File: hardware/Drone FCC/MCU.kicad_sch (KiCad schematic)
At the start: 38 parts, among them SW101 SW RESET, U101 STM32F746ZGTx, Y101 12MHz, Y102 32.768kHz

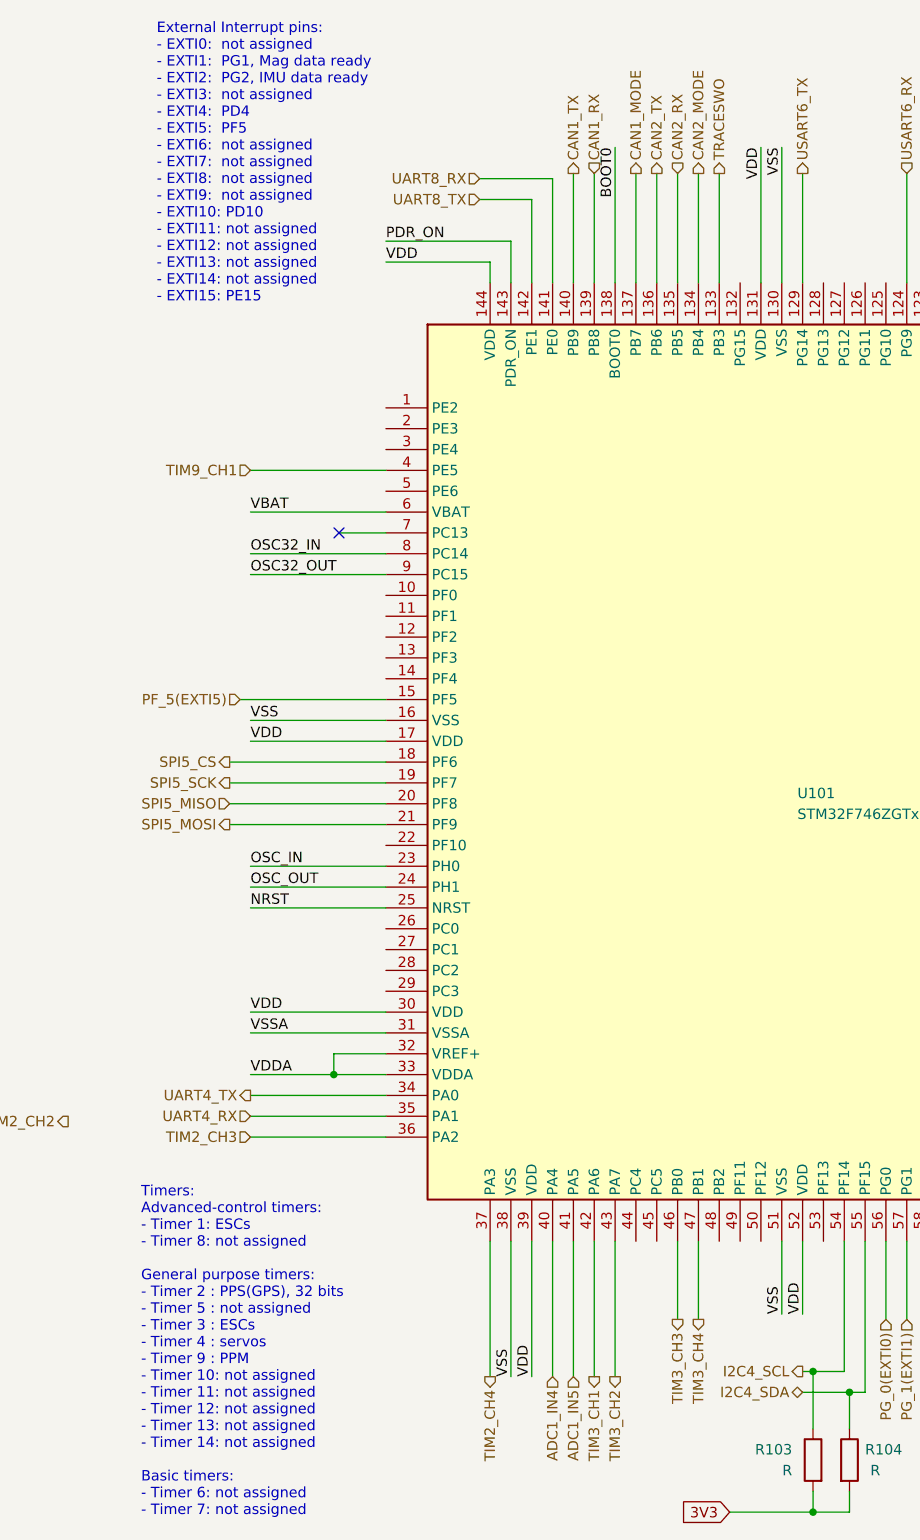
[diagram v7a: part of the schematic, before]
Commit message: added LEDs in routing
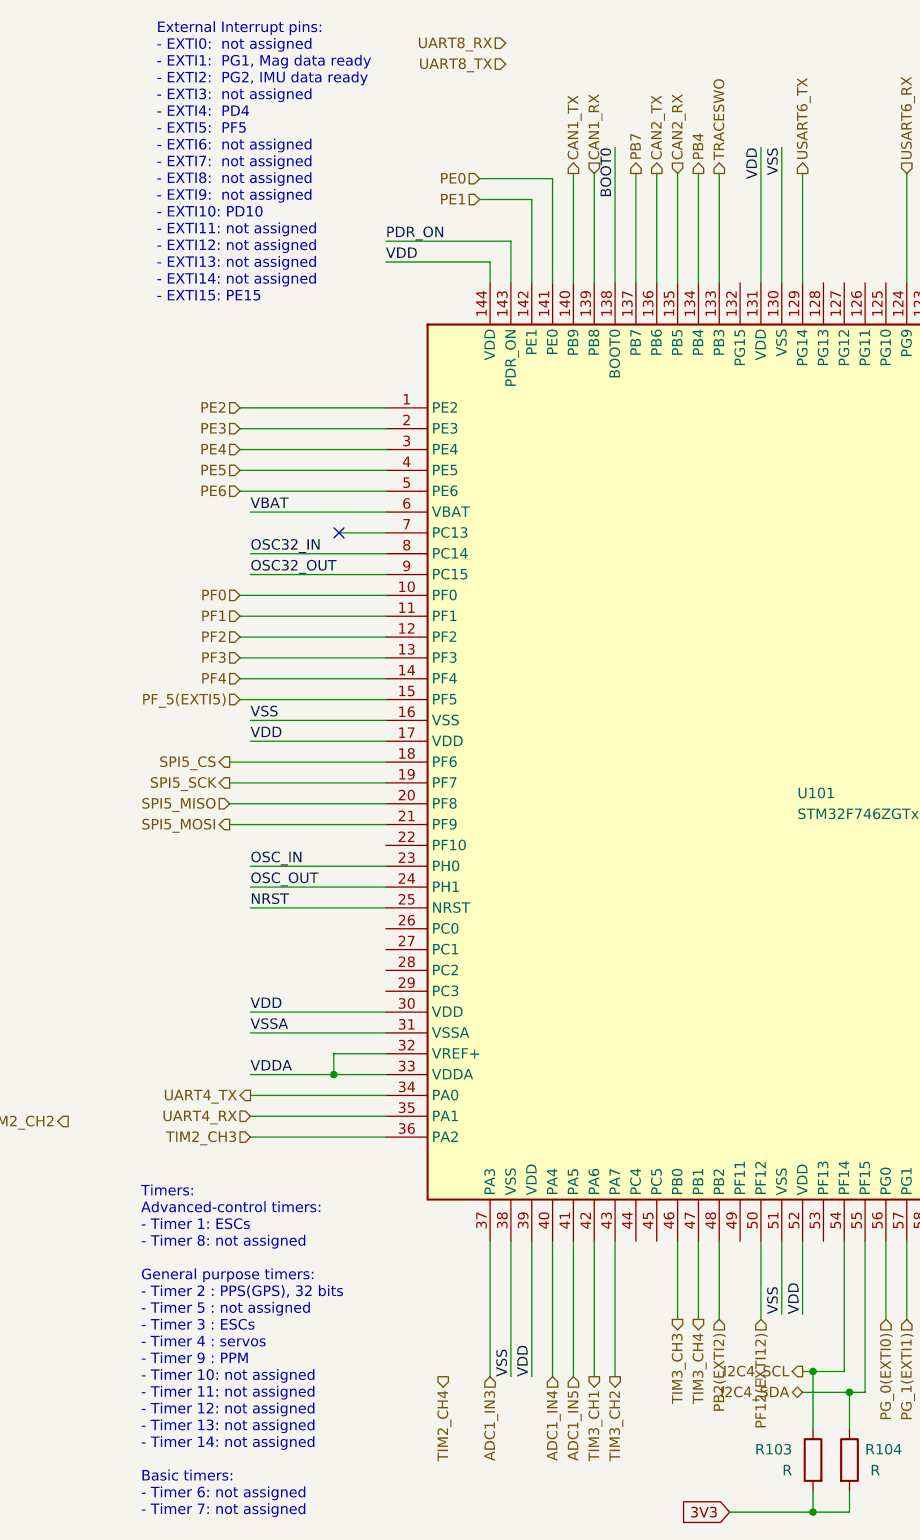
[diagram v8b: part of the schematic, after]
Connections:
- net TIM2_CH4: no longer U101.37 (PA3)
- net UART8_RX: no longer U101.141 (PE0)
- net UART8_TX: no longer U101.142 (PE1)
- net PE2: now reaches U101.1 (PE2)
- net PF0: now reaches U101.10 (PF0)
- net PF1: now reaches U101.11 (PF1)
- net PF2: now reaches U101.12 (PF2)
- net PF3: now reaches U101.13 (PF3)
- net PF4: now reaches U101.14 (PF4)
- net PE3: now reaches U101.2 (PE3)
- net PE4: now reaches U101.3 (PE4)
- net PB2(EXTI2): now reaches U101.48 (PB2)
- net PE6: now reaches U101.5 (PE6)
- net PF12(EXTI12): now reaches U101.50 (PF12)
- net CAN1_MODE renamed PB7
- net CAN2_MODE renamed PB4
- net TIM9_CH1 renamed PE5
- new net ADC1_IN3: U101.37 (PA3)
- new net PE0: U101.141 (PE0)
- new net PE1: U101.142 (PE1)
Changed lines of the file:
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@@
+    (stroke (width 0) (type default) (color 0 0 0 0))
+  )
+  (wire (pts (xy 25.4 66.04) (xy 43.18 66.04))
     (stroke (width 0) (type default) (color 0 0 0 0))
   )
@@
     (stroke (width 0) (type default) (color 0 0 0 0))
   )
+  (wire (pts (xy 25.4 93.98) (xy 43.18 93.98))
+    (stroke (width 0) (type default) (color 0 0 0 0))
+  )
   (wire (pts (xy 139.7 195.58) (xy 149.225 195.58))
     (stroke (width 0) (type default) (color 0 0 0 0))
@@
     (stroke (width 0) (type default) (color 0 0 0 0))
   )
+  (wire (pts (xy 83.82 162.56) (xy 83.82 172.085))
+    (stroke (width 0) (type default) (color 0 0 0 0))
+  )
   (wire (pts (xy 93.98 162.56) (xy 93.98 171.45))
     (stroke (width 0) (type default) (color 0 0 0 0))
@@
     (stroke (width 0) (type default) (color 0 0 0 0))
   )
+  (wire (pts (xy 25.4 60.96) (xy 43.18 60.96))
+    (stroke (width 0) (type default) (color 0 0 0 0))
+  )
   (wire (pts (xy 58.42 179.07) (xy 58.42 162.56))
     (stroke (width 0) (type default) (color 0 0 0 0))
@@
     (stroke (width 0) (type default) (color 0 0 0 0))
   )
+  (wire (pts (xy 88.9 162.56) (xy 88.9 172.085))
+    (stroke (width 0) (type default) (color 0 0 0 0))
+  )
   (wire (pts (xy 274.32 81.915) (xy 274.32 83.82))
     (stroke (width 0) (type default) (color 0 0 0 0))
@@
     (stroke (width 0) (type default) (color 0 0 0 0))
   )
+  (wire (pts (xy 25.4 86.36) (xy 43.18 86.36))
+    (stroke (width 0) (type default) (color 0 0 0 0))
+  )
   (wire (pts (xy 259.08 49.53) (xy 270.51 49.53))
     (stroke (width 0) (type default) (color 0 0 0 0))
@@
     (stroke (width 0) (type default) (color 0 0 0 0))
   )
+  (wire (pts (xy 25.4 71.12) (xy 43.18 71.12))
+    (stroke (width 0) (type default) (color 0 0 0 0))
+  )
   (wire (pts (xy 270.51 38.1) (xy 270.51 36.195))
     (stroke (width 0) (type default) (color 0 0 0 0))
@@
     (stroke (width 0) (type default) (color 0 0 0 0))
   )
-  (wire (pts (xy 26.67 68.58) (xy 43.18 68.58))
-    (stroke (width 0) (type default) (color 0 0 0 0))
-  )
   (wire (pts (xy 139.7 180.975) (xy 153.67 180.975))
     (stroke (width 0) (type default) (color 0 0 0 0))
@@
     (stroke (width 0) (type default) (color 0 0 0 0))
   )
+  (wire (pts (xy 25.4 91.44) (xy 43.18 91.44))
+    (stroke (width 0) (type default) (color 0 0 0 0))
+  )
   (wire (pts (xy 236.22 36.195) (xy 236.22 38.1))
     (stroke (width 0) (type default) (color 0 0 0 0))
@@
     (stroke (width 0) (type default) (color 0 0 0 0))
   )
+  (wire (pts (xy 25.4 88.9) (xy 43.18 88.9))
+    (stroke (width 0) (type default) (color 0 0 0 0))
+  )
   (polyline (pts (xy 202.565 112.395) (xy 204.47 112.395))
     (stroke (width 0) (type default) (color 0 0 0 0))
@@
     (stroke (width 0) (type default) (color 0 0 0 0))
   )
+  (wire (pts (xy 25.4 68.58) (xy 43.18 68.58))
+    (stroke (width 0) (type default) (color 0 0 0 0))
+  )
   (wire (pts (xy 165.735 29.845) (xy 173.99 29.845))
     (stroke (width 0) (type default) (color 0 0 0 0))
@@
     (stroke (width 0) (type default) (color 0 0 0 0))
   )
+  (wire (pts (xy 25.4 83.82) (xy 43.18 83.82))
+    (stroke (width 0) (type default) (color 0 0 0 0))
+  )
   (wire (pts (xy 203.835 17.78) (xy 203.835 20.955))
     (stroke (width 0) (type default) (color 0 0 0 0))
@@
   )
   (wire (pts (xy 154.94 73.66) (xy 168.275 73.66))
+    (stroke (width 0) (type default) (color 0 0 0 0))
+  )
+  (wire (pts (xy 25.4 63.5) (xy 43.18 63.5))
     (stroke (width 0) (type default) (color 0 0 0 0))
   )
@@
     (effects (font (size 1.27 1.27)) (justify left))
   )
+  (hierarchical_label "PE1" (shape input) (at 54.61 35.56 180)
+    (effects (font (size 1.27 1.27)) (justify right))
+  )
+  (hierarchical_label "PF0" (shape input) (at 25.4 83.82 180)
+    (effects (font (size 1.27 1.27)) (justify right))
+  )
   (hierarchical_label "SWDIO" (shape bidirectional) (at 168.275 68.58 0)
     (effects (font (size 1.27 1.27)) (justify left))
   )
-  (hierarchical_label "UART8_RX" (shape input) (at 54.61 33.02 180)
+  (hierarchical_label "PF2" (shape input) (at 25.4 88.9 180)
+    (effects (font (size 1.27 1.27)) (justify right))
+  )
+  (hierarchical_label "PE0" (shape input) (at 54.61 33.02 180)
+    (effects (font (size 1.27 1.27)) (justify right))
+  )
+  (hierarchical_label "UART8_RX" (shape input) (at 57.785 16.51 180)
     (effects (font (size 1.27 1.27)) (justify right))
   )
@@
     (effects (font (size 1.27 1.27)) (justify left))
   )
+  (hierarchical_label "PB2(EXTI2)" (shape input) (at 83.82 172.085 270)
+    (effects (font (size 1.27 1.27)) (justify right))
+  )
   (hierarchical_label "TIM3_CH4" (shape output) (at 81.28 172.085 270)
     (effects (font (size 1.27 1.27)) (justify right))
@@
     (effects (font (size 1.27 1.27)) (justify right))
   )
+  (hierarchical_label "ADC1_IN3" (shape input) (at 55.88 179.07 270)
+    (effects (font (size 1.27 1.27)) (justify right))
+  )
   (hierarchical_label "SDMMC1_CMD" (shape bidirectional) (at 127 32.385 90)
     (effects (font (size 1.27 1.27)) (justify left))
@@
     (effects (font (size 1.27 1.27)) (justify right))
   )
+  (hierarchical_label "PF3" (shape input) (at 25.4 91.44 180)
+    (effects (font (size 1.27 1.27)) (justify right))
+  )
   (hierarchical_label "OTG_FS_ID" (shape input) (at 168.275 76.2 0)
     (effects (font (size 1.27 1.27)) (justify left))
@@
     (effects (font (size 1.27 1.27)) (justify left))
   )
-  (hierarchical_label "TIM2_CH4" (shape output) (at 55.88 179.07 270)
+  (hierarchical_label "TIM2_CH4" (shape output) (at 50.165 179.07 270)
     (effects (font (size 1.27 1.27)) (justify right))
   )
@@
     (effects (font (size 1.27 1.27)) (justify left))
   )
-  (hierarchical_label "UART8_TX" (shape input) (at 54.61 35.56 180)
+  (hierarchical_label "PE6" (shape input) (at 25.4 71.12 180)
+    (effects (font (size 1.27 1.27)) (justify right))
+  )
+  (hierarchical_label "PF12(EXTI12)" (shape input) (at 88.9 172.085 270)
+    (effects (font (size 1.27 1.27)) (justify right))
+  )
+  (hierarchical_label "UART8_TX" (shape input) (at 57.785 19.05 180)
     (effects (font (size 1.27 1.27)) (justify right))
   )
@@
     (effects (font (size 1.27 1.27)) (justify right))
   )
-  (hierarchical_label "CAN2_MODE" (shape output) (at 81.28 32.385 90)
+  (hierarchical_label "PB4" (shape output) (at 81.28 32.385 90)
     (effects (font (size 1.27 1.27)) (justify left))
   )
@@
     (effects (font (size 1.27 1.27)) (justify left))
   )
+  (hierarchical_label "PF4" (shape input) (at 25.4 93.98 180)
+    (effects (font (size 1.27 1.27)) (justify right))
+  )
   (hierarchical_label "TIM1_CH3" (shape output) (at 129.54 172.085 270)
     (effects (font (size 1.27 1.27)) (justify right))
@@
     (effects (font (size 1.27 1.27)) (justify right))
   )
+  (hierarchical_label "PF1" (shape input) (at 25.4 86.36 180)
+    (effects (font (size 1.27 1.27)) (justify right))
+  )
   (hierarchical_label "USART3_TX" (shape output) (at 168.275 139.7 0)
     (effects (font (size 1.27 1.27)) (justify left))
@@
     (effects (font (size 1.27 1.27)) (justify left))
   )
-  (hierarchical_label "CAN1_MODE" (shape output) (at 73.66 32.385 90)
-    (effects (font (size 1.27 1.27)) (justify left))
+  (hierarchical_label "PB7" (shape output) (at 73.66 32.385 90)
+    (effects (font (size 1.27 1.27)) (justify left))
+  )
+  (hierarchical_label "PE5" (shape input) (at 25.4 68.58 180)
+    (effects (font (size 1.27 1.27)) (justify right))
   )
   (hierarchical_label "UART4_TX" (shape output) (at 26.67 144.78 180)
@@
     (effects (font (size 1.27 1.27)) (justify right))
   )
-  (hierarchical_label "TIM9_CH1" (shape input) (at 26.67 68.58 180)
+  (hierarchical_label "PE2" (shape input) (at 25.4 60.96 180)
+    (effects (font (size 1.27 1.27)) (justify right))
+  )
+  (hierarchical_label "PE4" (shape input) (at 25.4 66.04 180)
     (effects (font (size 1.27 1.27)) (justify right))
   )
@@
     (effects (font (size 1.27 1.27)) (justify right))
   )
+  (hierarchical_label "PE3" (shape input) (at 25.4 63.5 180)
+    (effects (font (size 1.27 1.27)) (justify right))
+  )
